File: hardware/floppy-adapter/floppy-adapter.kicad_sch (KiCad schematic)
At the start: 12 parts, among them J1 Conn_02x17 socket (O1 side), J2 Conn_02x17 header (OEM cable), J3 Conn_02x17 header (Gotek), J4 Gotek power, J5 Panel switch, K1 4PDT relay, 5V coil

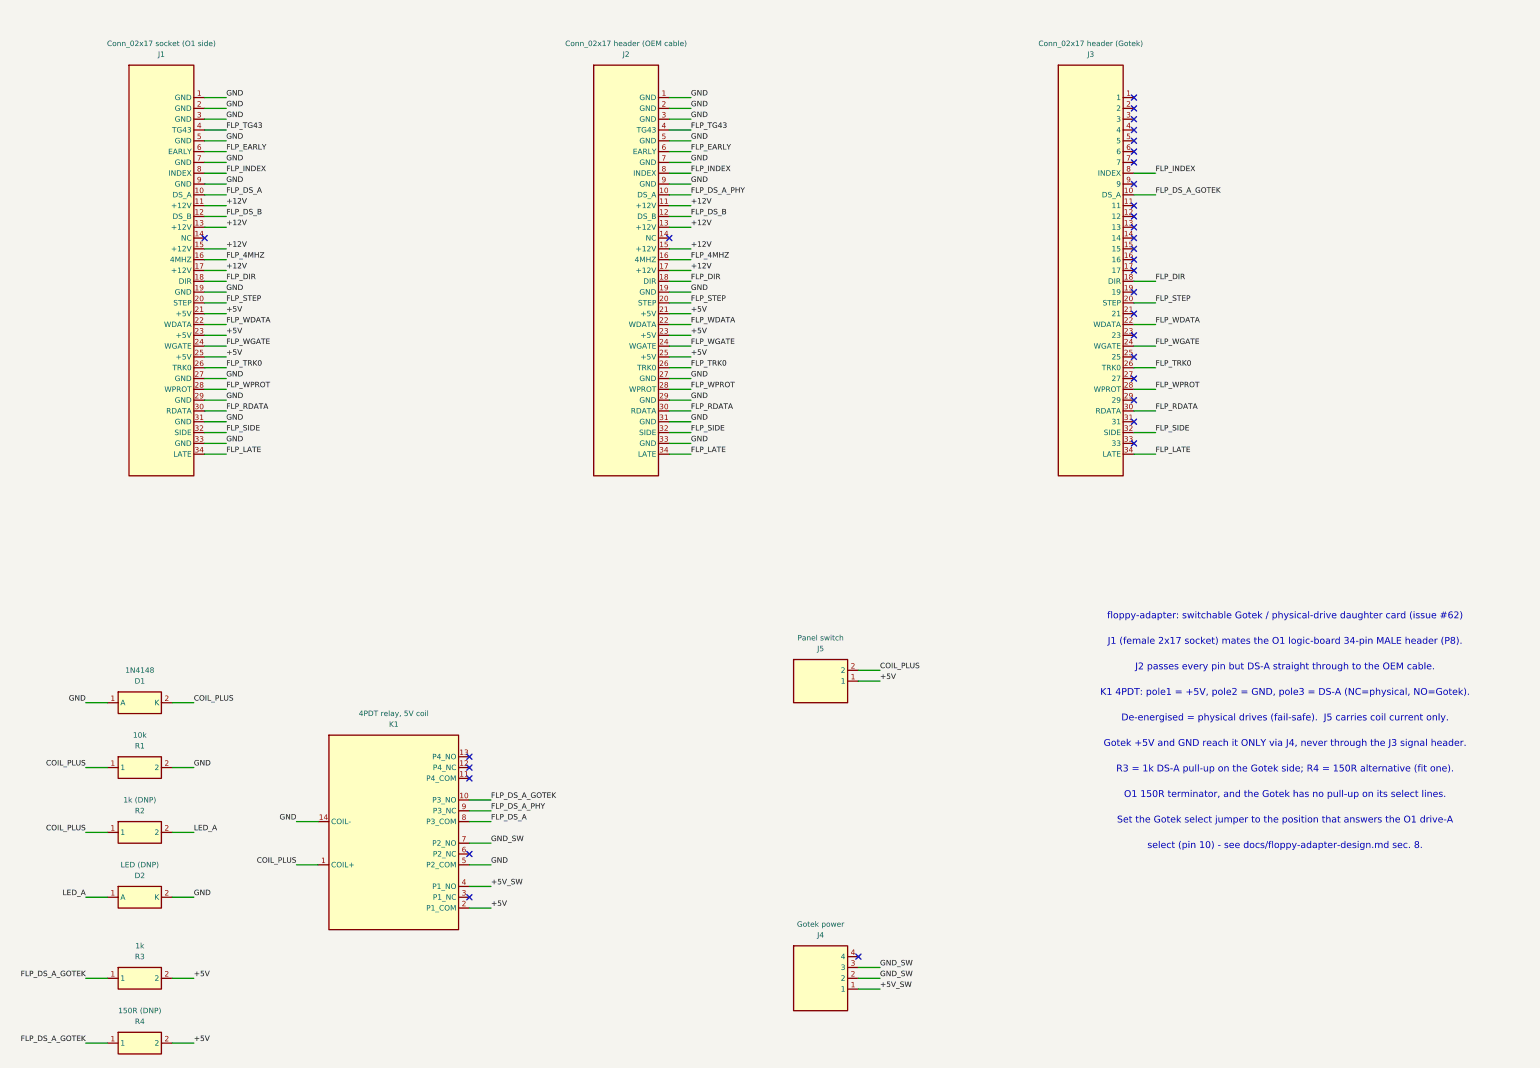
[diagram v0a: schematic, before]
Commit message: hardware: the floppy-adapter schematic, wired, footprinted, and switched with silicon (#62) (#349)
* hardware: draw the floppy-adapter's nets and give its parts footprints (#62)

The Rev A capture was a net *label* on every pin with no wire between any two
parts: a correct netlist and a drawing nobody could follow.  This is the same
treatment the WiFi COMM PAC got (#347), for the same reasons.

* Every net is routed as orthogonal segments on a 1.27 mm grid by the Manhattan
  A* that `../wifi-comm-pac/gen_wifi_comm_pac_sch.py` uses -- copied, not
  imported, because tools/check_schematics.py regenerates each board's sheet by
  running its generator **alone in a scratch directory**.
* **One label per signal net** (21 of them) keeps the names.  One and not
  fifteen is the safety property: a missing wire breaks the netlist instead of
  being hidden by a label doing the connecting.
* GND/+5V/+12V are routed like signals with **one power symbol each** and a
  PWR_FLAG, not a symbol per pin -- GND lands on eleven pins of J1 and +12V on
  four consecutive ones, and 3.81 mm glyphs 2.54 mm apart stack on top of each
  other.
* **11 of 12 footprints assigned**, from KiCad's own libraries and
  through-hole throughout: this is the board a person builds by hand, and
  `Update PCB from Schematic` transfers nothing for an empty Footprint field.
  K1 is deliberately open (see the next commit): the 4PDT DIP relay class is
  obsolete and a footprint for the wrong package is a board that does not fit.

Two defects came out of it, both found by comparing netlists rather than by
looking at the sheet:

* **A wire ended on a no-connect pin.**  The router blocked other nets' pins
  but not the ones marked no-connect -- they carry no net, so they are not in
  the net-holding table -- and the first wired netlist grew J3.14 and K1.11 onto
  FLP_DS_A_GOTEK.  A no-connect marker says the pin goes nowhere; the netlist
  believes the wire.
* **The checker's floppy pinout table contradicted the d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
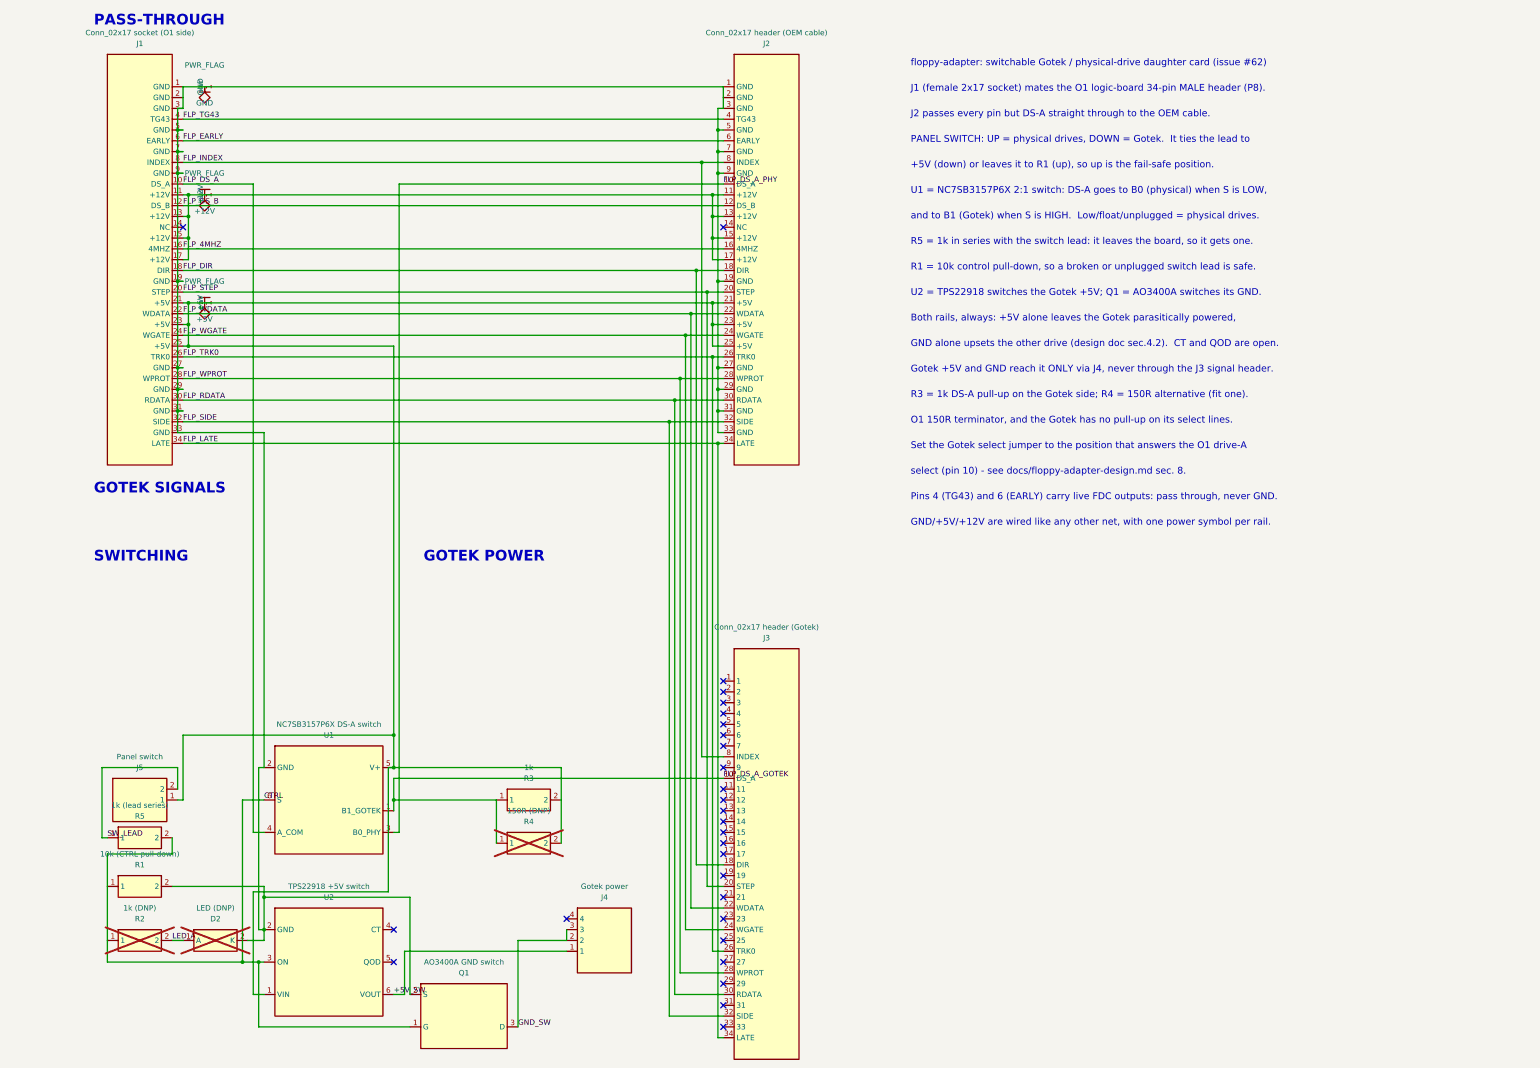
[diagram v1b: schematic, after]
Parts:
- removed D1: 1N4148, symbol local:DIODE
- removed K1: 4PDT relay, 5V coil, symbol local:RELAY_4PDT
- added Q1: AO3400A GND switch, Package_TO_SOT_SMD:SOT-23, symbol local:NFET_GSD
- added R5: 1k (lead series), Resistor_THT:R_Axial_DIN0207_L6.3mm_D2.5mm_P7.62mm_Horizontal, symbol local:RES
- added U1: NC7SB3157P6X DS-A switch, Package_TO_SOT_SMD:SOT-363_SC-70-6, symbol local:BUS_SW_2TO1
- added U2: TPS22918 +5V switch, Package_TO_SOT_SMD:SOT-23-6, symbol local:LOAD_SW
- D2: footprint (none) -> LED_THT:LED_D5.0mm; now not fitted; now left out of the parts list
- J1: footprint (none) -> Connector_PinSocket_2.54mm:PinSocket_2x17_P2.54mm_Vertical
- J2, J3: footprint (none) -> Connector_IDC:IDC-Header_2x17_P2.54mm_Vertical
- J4: footprint (none) -> Connector_PinHeader_2.54mm:PinHeader_1x04_P2.54mm_Horizontal
- J5: footprint (none) -> Connector_PinHeader_2.54mm:PinHeader_1x02_P2.54mm_Vertical
- R1: value 10k -> 10k (CTRL pull-down); footprint (none) -> Resistor_THT:R_Axial_DIN0207_L6.3mm_D2.5mm_P7.62mm_Horizontal
- R2, R4: footprint (none) -> Resistor_THT:R_Axial_DIN0207_L6.3mm_D2.5mm_P7.62mm_Horizontal; now not fitted; now left out of the parts list
- R3: footprint (none) -> Resistor_THT:R_Axial_DIN0207_L6.3mm_D2.5mm_P7.62mm_Horizontal
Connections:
- net +5V: now also U1.5 (V+), U2.1 (VIN)
- net +5V_SW: now also U2.6 (VOUT)
- net FLP_DS_A: now also U1.4 (A_COM)
- net FLP_DS_A_GOTEK: now also U1.1 (B1_GOTEK)
- net FLP_DS_A_PHY: now also U1.3 (B0_PHY)
- net GND: now also Q1.2 (S), U1.2 (GND), U2.2 (GND)
- net GND_SW: now also Q1.3 (D)
- net COIL_PLUS renamed CTRL
- net CTRL: now also Q1.1 (G), R5.2, U1.6 (S), U2.3 (ON); no longer J5.2
- new net SW_LEAD: J5.2, R5.1
- no-connect marks 31 -> 28
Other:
- note added: "+5V (down) or leaves it to R1 (up), so up is the fail-safe position."
- note added: "Both rails, always: +5V alone leaves the Gotek parasitically powered,"
- note added: "GND alone upsets the other drive (design doc sec.4.2). CT and QOD are open."
- note added: "GND/+5V/+12V are wired like any other net, with one power symbol per rail."
- note added: "GOTEK POWER"
- note added: "GOTEK SIGNALS"
- note added: "PANEL SWITCH: UP = physical drives, DOWN = Gotek. It ties the lead to"
- note added: "PASS-THROUGH"
- note added: "Pins 4 (TG43) and 6 (EARLY) carry live FDC outputs: pass through, never GND."
- note added: "R1 = 10k control pull-down, so a broken or unplugged switch lead is safe."
- note added: "R5 = 1k in series with the switch lead: it leaves the board, so it gets one."
- note added: "SWITCHING"
- note added: "U1 = NC7SB3157P6X 2:1 switch: DS-A goes to B0 (physical) when S is LOW,"
- note added: "U2 = TPS22918 switches the Gotek +5V; Q1 = AO3400A switches its GND."
- note added: "and to B1 (Gotek) when S is HIGH. Low/float/unplugged = physical drives."
- note removed: "De-energised = physical drives (fail-safe). J5 carries coil current only."
- note removed: "K1 4PDT: pole1 = +5V, pole2 = GND, pole3 = DS-A (NC=physical, NO=Gotek)."
